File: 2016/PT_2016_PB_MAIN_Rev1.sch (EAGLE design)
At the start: 113 parts, among them Q1 Q_IRFS7437PbF, Q11 Q_IRFS7437PbF, Q12 2N7002, Q14 Q_IRFS7437PbF, Q16 Q_IRFS7437PbF, Q20 Q_IRFS7437PbF, Q6 Q_IRFS7437PbF, Q7 Q_IRFS7437PbF, Q9 Q_IRFS7437PbF

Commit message: Added Murata 5V Converter and TI uC
Rearranged board
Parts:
- removed 12V-CRIT: H_WR-TBL_3210002HORIZ, MRDT-2015-PowerBoard:H_WR-TBL_3210002HORIZ
- removed JP1: (no value), jumper:JP1E
- removed LED13: (no value), SparkFun-LED:LED-FKIT-1206
- removed LED3: (no value), SparkFun-LED:LED1206
- removed R11: 1kΩ, SparkFun-Passives:RESISTOR1206
- removed R2: 10k Ohm, SparkFun-Passives:RESISTOR1206
- added C10: 1uF, resistor:C-USC1206
- added OKI-78SR-5/1.5-W36H: Q_OKI-78SR, MRDT-2015-PowerBoard:Q_OKI-78SR
- added R6: 120 Ohm, SparkFun-Passives:RESISTOR1206
- added U$12: MAX3077, MAX3077:MAX3077
- added U$23, U$5: RJ45-8PTH, SparkFun-Connectors:RJ45-8PTH
- added U$3: MURATA_5V_DC-DC_CONVERTER, Murata_5V_DC-DC_Converter:MURATA_5V_DC-DC_CONVERTER
- added U$4: TIVA-C-CONNECTED, MRDT-2015-General:TIVA-C-CONNECTED
- R1: value 1k Ohm -> 120 Ohm
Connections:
- removed net 12V-CRIT: 12V-CRIT.R, LED3.A
- removed net INFO_LED: R1.1
- removed net JUMPER_SIG_IN: JP1.1, R2.1
- removed net N$11: LED13.A, R1.2
- new net N$18: R6.1, U$12.Z, U$5.2
- new net N$19: R1.2, U$12.B, U$5.6
- new net N$20: R1.1, U$12.A, U$5.3
- new net N$21: U$12.DI
- new net RXD: U$12.R0
- net +5V: now also C10.1, U$12.VCC; no longer R2.2
- net GND: now also C10.2, U$12.GND, U$5.7, U$5.8; no longer 12V-CRIT.L, JP1.2, LED13.C, R11.2
- net N$3: now also R6.2, U$12.Y, U$5.1; no longer LED3.C, R11.1
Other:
- moved on the sheet: 5V-INT, LED5, R1, R13

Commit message: Added final components and started routing.
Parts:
- added 5V-AUX: H_20020618-M02HORIZ, MRDT-2015-PowerBoard:H_20020618-M02HORIZ
- added LED3: (no value), SparkFun-LED:LED1206
- added R2, R7: 120 Ohm, SparkFun-Passives:RESISTOR1206
- added R8: 1kΩ, SparkFun-Passives:RESISTOR1206
- added U$24: MAX3077, MAX3077:MAX3077
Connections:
- new net 5V-AUX: 5V-AUX.R, R8.1
- new net 5V_AUX: U$3.+VOUT
- new net AUX_P2-IMEAS: U$2.VIOUT, U$4.PM6
- new net AUX_P2-SIG: U$1.IN, U$4.PD2
- new net N$100: U$4.RST
- new net N$101: U$4.PB2
- new net N$102: U$4.PB3
- new net N$105: U$4.PD0
- new net N$106: U$4.PD1
- new net N$108: U$4.PD3
- new net N$109: U$4.PD4
- new net N$11: R2.2, U$23.6, U$24.B
- new net N$110: U$4.PD5
- new net N$111: U$4.PD7
- new net N$112: U$4.PE0
- new net N$113: U$4.PE1
- new net N$115: U$4.PE2
- new net N$116: U$4.PE3
- new net N$117: U$4.PE4
- new net N$118: U$4.PE5
- new net N$119: U$4.PG0
- new net N$120: U$4.PG1
- new net N$121: U$4.PL0
- new net N$122: U$4.PL1
- new net N$123: U$4.PL2
- new net N$124: U$4.PL3
- new net N$125: U$4.PL4
- new net N$126: U$4.PL5
- new net N$127: U$4.PN2
- new net N$128: U$4.PN3
- new net N$129: U$4.PN4
- new net N$130: U$4.PN5
- new net N$131: U$4.PQ0
- new net N$133: U$4.PQ2/PA3
- new net N$134: U$4.PQ3/PA2
- new net N$32: R2.1, U$23.3, U$24.A
- new net N$33: U$24.DI
- new net N$34: LED3.A, R8.2
- new net N$35: U$4.PA4
- new net N$36: U$4.PA5
- new net N$37: U$4.PA6
- new net N$43: U$4.PC4
- new net N$48: U$4.PC5
- new net N$5: R7.2, U$23.1, U$24.Y
- new net N$50: U$4.PC6
- new net N$51: U$4.PC7
- new net N$52: U$4.PF1
- new net N$53: U$4.PF2
- new net N$58: U$4.PF3
- new net N$65: U$4.PH2
- new net N$70: U$4.PH3
- new net N$75: U$4.PK4
- new net N$76: U$4.PK5
- new net N$8: R7.1, U$23.2, U$24.Z
- new net N$83: U$4.PM0
- new net N$84: U$4.PM1
- new net N$85: U$4.PM2
- new net N$86: U$4.PM3
- new net N$87: U$4.PM4
- new net N$88: U$4.PM5
- new net N$90: U$4.PM7
- new net N$91: U$4.PP0
- new net N$92: U$4.PP1
- new net N$93: U$4.PP2
- new net N$97: U$4.+5V
- new net N$98: U$4.+3V3
- new net N$99: U$4.GND
- new net RXD1: U$24.R0
- net +5V: now also OKI-78SR-5/1.5-W36H.VO, U$24.VCC
- net AUX_P-IMEAS: now also U$4.PK7; no longer U$2.VIOUT
- net AUX_P-SIG: now also U$4.PB4; no longer U$1.IN
- net GND: now also 5V-AUX.L, LED3.C, OKI-78SR-5/1.5-W36H.GND, U$23.7, U$23.8, U$24.GND, U$3.-VIN, U$3.-VOUT
- net M1-IMEAS: now also U$4.PA7
- net M1-SIG: now also U$4.PP4
- net M2-IMEAS: now also U$4.PH0
- net M2-SIG: now also U$4.PK3
- net M3-IMEAS: now also U$4.PH1
- net M3-SIG: now also U$4.PK2
- net M4-IMEAS: now also U$4.PP3
- net M4-SIG: now also U$4.PK1
- net M5-IMEAS: now also U$4.PK6
- net M5-SIG: now also U$4.PK0
- net M6-IMEAS: now also U$4.PQ1
- net M6-SIG: now also U$4.PB5
- net V_BATT: now also OKI-78SR-5/1.5-W36H.VI, U$3.+VIN
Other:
- moved on the sheet: C10, OKI-78SR-5/1.5-W36H, U$23, U$3

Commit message: Continued routing, rearranged some things
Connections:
- removed net 5V_AUX: U$3.+VOUT
- removed net N$21: U$12.DI
- removed net N$33: U$24.DI
- removed net N$43: U$4.PC4
- removed net N$48: U$4.PC5
- removed net N$65: U$4.PH2
- removed net N$91: U$4.PP0
- removed net N$92: U$4.PP1
- removed net N$93: U$4.PP2
- removed net N$97: U$4.+5V
- removed net N$99: U$4.GND
- removed net RXD: U$12.R0
- removed net RXD1: U$24.R0
- new net RX1: U$12.R0, U$4.PC4
- new net RX2: U$24.R0, U$4.PP0
- new net TX1: U$12.DI, U$4.PC5
- new net TX2: U$24.DI, U$4.PP1
- net +5V: now also U$4.+5V
- net 12V-IMEAS: now also U$4.PH2
- net 5V-AUX: now also U$3.+VOUT
- net GND: now also U$4.GND
- net PRIMARY-VMEAS: now also U$4.PP2
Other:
- moved on the sheet: C10, OKI-78SR-5/1.5-W36H, R1, R2, R6, R7, U$23, U$5

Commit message: Routesss
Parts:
- removed U$22: TEST, MRDT-2015-General:TEST
- renumbered PALPATINE-12V to POE-12V, SIDEOUS-12V to FINN-12V, U$3 to REY-5V
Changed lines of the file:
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@@
 </classes>
 <parts>
-<part name="SIDEOUS-12V" library="MRDT-2015-PowerBoard" deviceset="UQW-12/20-T48NBS" device=""/>
-<part name="PALPATINE-12V" library="MRDT-2015-PowerBoard" deviceset="UQW-12/20-T48NBS" device=""/>
+<part name="FINN-12V" library="MRDT-2015-PowerBoard" deviceset="UQW-12/20-T48NBS" device=""/>
+<part name="POE-12V" library="MRDT-2015-PowerBoard" deviceset="UQW-12/20-T48NBS" device=""/>
 <part name="GND3" library="SparkFun-Aesthetics" deviceset="GND" device=""/>
 <part name="GND4" library="SparkFun-Aesthetics" deviceset="GND" device=""/>
@@
 <part name="P+25" library="supply1" deviceset="+5V" device=""/>
 <part name="GND95" library="SparkFun-Aesthetics" deviceset="GND" device=""/>
-<part name="U$22" library="MRDT-2015-General" deviceset="TEST" device=""/>
 <part name="SUPPLY2" library="SparkFun-Aesthetics" deviceset="V_BATT" device=""/>
 <part name="Q1" library="MRDT-2015-PowerBoard" deviceset="Q_IRF*7437" device="SMD" value="Q_IRFS7437PbF"/>
@@
 <part name="C9" library="resistor" deviceset="C-US" device="C1206" value="1nF"/>
 <part name="GND13" library="SparkFun-Aesthetics" deviceset="GND" device=""/>
-<part name="U$3" library="Murata_5V_DC-DC_Converter" deviceset="MURATA_5V_DC-DC_CONVERTER" device=""/>
+<part name="REY-5V" library="Murata_5V_DC-DC_Converter" deviceset="MURATA_5V_DC-DC_CONVERTER" device=""/>
 <part name="U$4" library="MRDT-2015-General" deviceset="TIVA-C-CONNECTED" device=""/>
 <part name="U$5" library="SparkFun-Connectors" deviceset="RJ45-8" device="PTH"/>
@@
 </plain>
 <instances>
-<instance part="SIDEOUS-12V" gate="G$1" x="63.5" y="73.66"/>
-<instance part="PALPATINE-12V" gate="G$1" x="63.5" y="43.18"/>
+<instance part="FINN-12V" gate="G$1" x="63.5" y="73.66"/>
+<instance part="POE-12V" gate="G$1" x="63.5" y="43.18"/>
 <instance part="GND3" gate="1" x="35.56" y="30.48"/>
 <instance part="GND4" gate="1" x="35.56" y="60.96"/>
@@
 <instance part="P+25" gate="1" x="226.06" y="91.44"/>
 <instance part="GND95" gate="1" x="226.06" y="66.04"/>
-<instance part="U$22" gate="G$1" x="-1163.32" y="-378.46"/>
 <instance part="SUPPLY2" gate="G$1" x="-518.16" y="231.14"/>
 <instance part="Q1" gate="G$1" x="-520.7" y="182.88"/>
@@
 <instance part="C9" gate="G$1" x="-474.98" y="203.2"/>
 <instance part="GND13" gate="1" x="-487.68" y="231.14"/>
-<instance part="U$3" gate="G$1" x="109.22" y="129.54"/>
+<instance part="REY-5V" gate="G$1" x="109.22" y="129.54"/>
 <instance part="U$4" gate="G$1" x="-162.56" y="-147.32"/>
 <instance part="U$5" gate="G$1" x="-462.28" y="-53.34" rot="R180"/>
@@
 <net name="GND" class="0">
 <segment>
-<pinref part="SIDEOUS-12V" gate="G$1" pin="-VIN"/>
+<pinref part="FINN-12V" gate="G$1" pin="-VIN"/>
 <pinref part="GND4" gate="1" pin="GND"/>
 <wire x1="40.64" y1="66.04" x2="35.56" y2="66.04" width="0.1524" layer="91"/>
@@
 </segment>
 <segment>
-<pinref part="PALPATINE-12V" gate="G$1" pin="-VIN"/>
+<pinref part="POE-12V" gate="G$1" pin="-VIN"/>
 <wire x1="40.64" y1="35.56" x2="35.56" y2="35.56" width="0.1524" layer="91"/>
 <wire x1="35.56" y1="35.56" x2="35.56" y2="33.02" width="0.1524" layer="91"/>
@@
 </segment>
 <segment>
-<pinref part="SIDEOUS-12V" gate="G$1" pin="-VOUT"/>
+<pinref part="FINN-12V" gate="G$1" pin="-VOUT"/>
 <pinref part="GND11" gate="1" pin="GND"/>
 </segment>
 <segment>
-<pinref part="PALPATINE-12V" gate="G$1" pin="-VOUT"/>
+<pinref part="POE-12V" gate="G$1" pin="-VOUT"/>
 <pinref part="GND12" gate="1" pin="GND"/>
 </segment>
@@
 </segment>
 <segment>
-<pinref part="U$3" gate="G$1" pin="-VIN"/>
+<pinref part="REY-5V" gate="G$1" pin="-VIN"/>
 <pinref part="GND19" gate="1" pin="GND"/>
 <wire x1="93.98" y1="127" x2="76.2" y2="127" width="0.1524" layer="91"/>
 <wire x1="76.2" y1="127" x2="76.2" y2="124.46" width="0.1524" layer="91"/>
-<pinref part="U$3" gate="G$1" pin="-VOUT"/>
+<pinref part="REY-5V" gate="G$1" pin="-VOUT"/>
 <wire x1="76.2" y1="124.46" x2="76.2" y2="121.92" width="0.1524" layer="91"/>
 <wire x1="93.98" y1="124.46" x2="76.2" y2="124.46" width="0.1524" layer="91"/>
@@
 <pinref part="SUPPLY3" gate="G$1" pin="V_BATT"/>
 <wire x1="35.56" y1="81.28" x2="35.56" y2="83.82" width="0.1524" layer="91"/>
-<pinref part="SIDEOUS-12V" gate="G$1" pin="+VIN"/>
+<pinref part="FINN-12V" gate="G$1" pin="+VIN"/>
 <wire x1="35.56" y1="81.28" x2="40.64" y2="81.28" width="0.1524" layer="91"/>
 </segment>
@@
 <wire x1="33.02" y1="50.8" x2="33.02" y2="53.34" width="0.1524" layer="91"/>
 <junction x="33.02" y="50.8"/>
-<pinref part="PALPATINE-12V" gate="G$1" pin="+VIN"/>
+<pinref part="POE-12V" gate="G$1" pin="+VIN"/>
 <junction x="33.02" y="50.8"/>
 <wire x1="40.64" y1="50.8" x2="33.02" y2="50.8" width="0.1524" layer="91"/>
@@
 </segment>
 <segment>
-<pinref part="U$3" gate="G$1" pin="+VIN"/>
+<pinref part="REY-5V" gate="G$1" pin="+VIN"/>
 <pinref part="SUPPLY5" gate="G$1" pin="V_BATT"/>
 <wire x1="93.98" y1="132.08" x2="76.2" y2="132.08" width="0.1524" layer="91"/>
@@
 <net name="N$4" class="0">
 <segment>
-<pinref part="PALPATINE-12V" gate="G$1" pin="REMOTE"/>
+<pinref part="POE-12V" gate="G$1" pin="REMOTE"/>
 <wire x1="40.64" y1="43.18" x2="15.24" y2="43.18" width="0.1524" layer="91"/>
 <wire x1="15.24" y1="43.18" x2="15.24" y2="58.42" width="0.1524" layer="91"/>
-<pinref part="SIDEOUS-12V" gate="G$1" pin="REMOTE"/>
+<pinref part="FINN-12V" gate="G$1" pin="REMOTE"/>
 <wire x1="15.24" y1="58.42" x2="15.24" y2="73.66" width="0.1524" layer="91"/>
 <wire x1="15.24" y1="73.66" x2="40.64" y2="73.66" width="0.1524" layer="91"/>
@@
 <net name="N$7" class="0">
 <segment>
-<pinref part="PALPATINE-12V" gate="G$1" pin="+VOUT"/>
+<pinref part="POE-12V" gate="G$1" pin="+VOUT"/>
 <wire x1="88.9" y1="50.8" x2="96.52" y2="50.8" width="0.1524" layer="91"/>
 <wire x1="96.52" y1="50.8" x2="96.52" y2="53.34" width="0.1524" layer="91"/>
-<pinref part="SIDEOUS-12V" gate="G$1" pin="+VOUT"/>
+<pinref part="FINN-12V" gate="G$1" pin="+VOUT"/>
 <wire x1="96.52" y1="53.34" x2="96.52" y2="81.28" width="0.1524" layer="91"/>
 <wire x1="96.52" y1="81.28" x2="88.9" y2="81.28" width="0.1524" layer="91"/>
@@
 </segment>
 <segment>
-<pinref part="U$3" gate="G$1" pin="+VOUT"/>
+<pinref part="REY-5V" gate="G$1" pin="+VOUT"/>
 <wire x1="127" y1="132.08" x2="132.08" y2="132.08" width="0.1524" layer="91"/>
 <label x="132.08" y="132.08" size="1.778" layer="95" xref="yes"/>

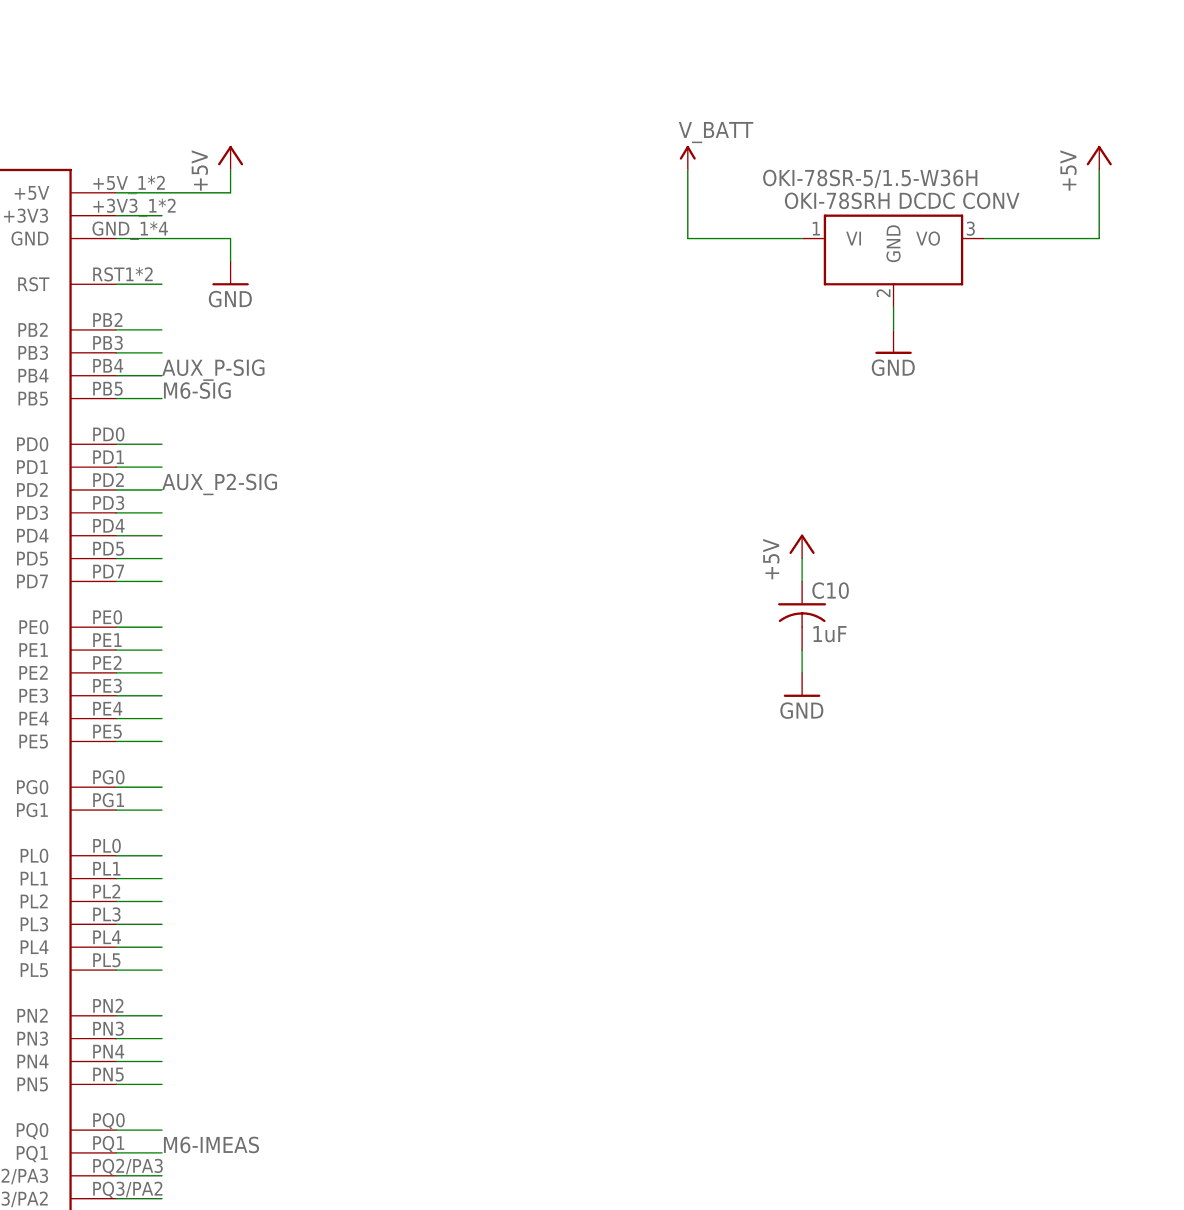
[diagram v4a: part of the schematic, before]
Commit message: Minor routing changes
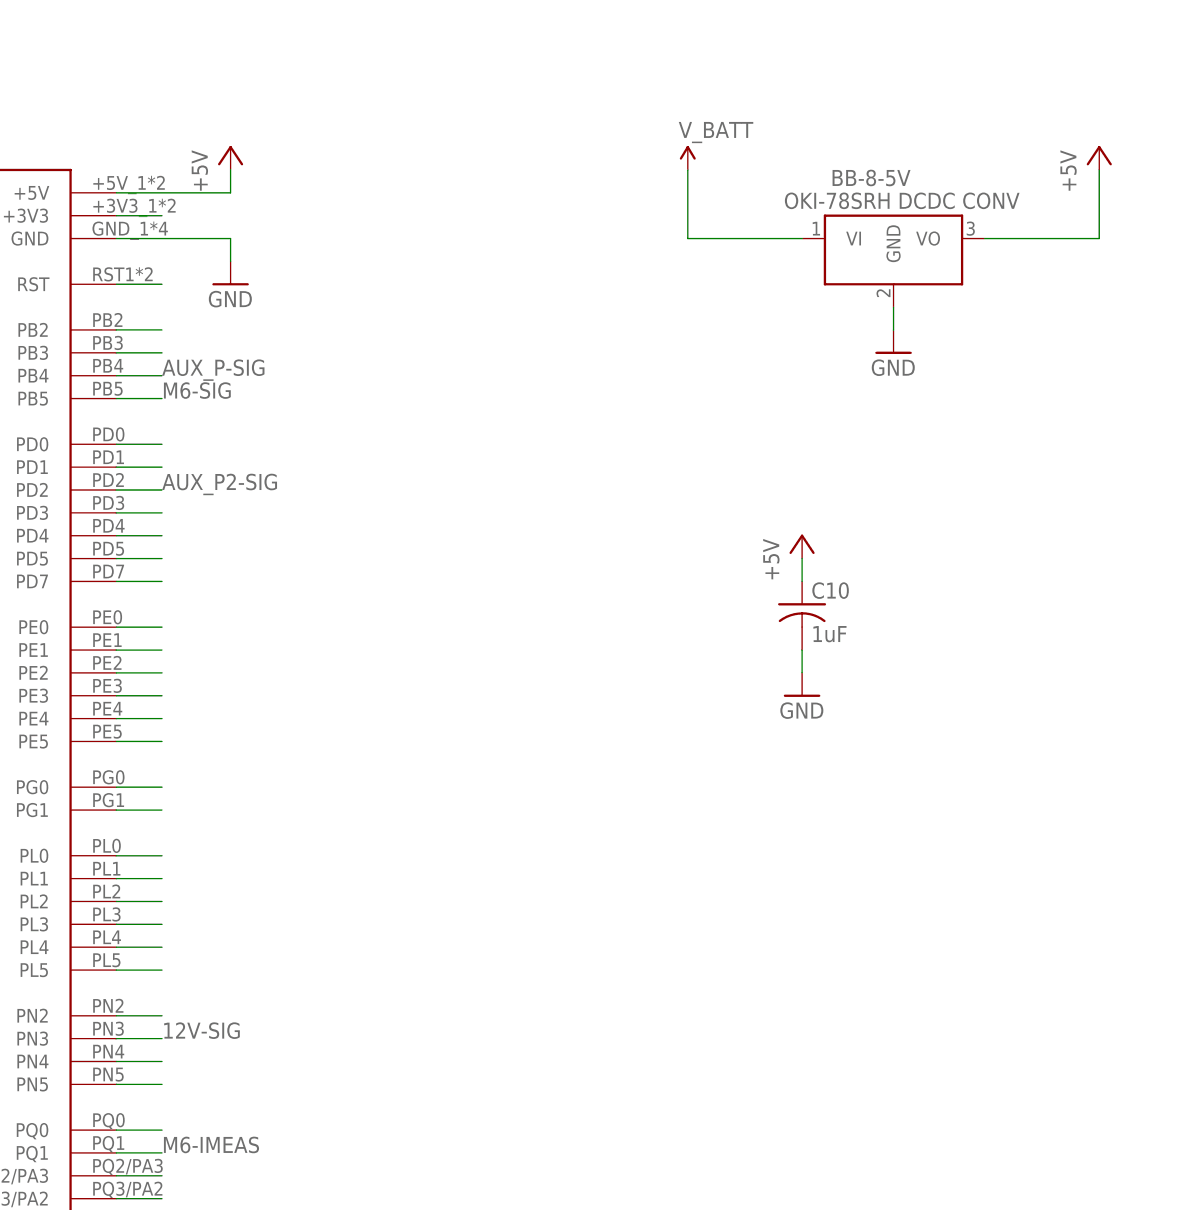
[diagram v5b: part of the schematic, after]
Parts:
- renumbered OKI-78SR-5/1.5-W36H to BB-8-5V
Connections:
- removed net N$128: U$4.PN3
- net 12V-SIG: now also U$4.PN3

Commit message: Rearranged components and routing
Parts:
- added C11: .1µF, resistor:C-USC1206
- added C12: 1nF, resistor:C-USC1206
- added C22: 10µF, resistor:CPOL-USE5-8.5
- added Q2: 2N7002, SparkFun-DiscreteSemi:MOSFET-NCHANNEL2N7002PW
- added R11: 1k, resistor:R-US_R1206
- added U$3: ACS714LLCTR-50A-T, MRDT-2015-PowerBoard:Q_ACS714
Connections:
- removed net N$105: U$4.PD0
- removed net N$106: U$4.PD1
- removed net N$109: U$4.PD4
- removed net N$111: U$4.PD7
- new net 5V-IMEAS: U$3.VIOUT, U$4.PD0
- new net 5V-SIG: R11.2, U$4.PN3
- new net N$38: C12.1, U$3.FILTER
- new net N$43: Q2.D, REY-5V.ON/OFF
- new net N$48: Q2.G, R11.1
- new net N$7: C22.+, REY-5V.+SENSE, REY-5V.+VOUT, U$3.IP+
- new net N$70: U$4.PH2
- new net N$89: U$4.PM6
- new net N$93: U$4.PP4
- net +5V: now also C11.2, U$3.VCC
- net 12V-IMEAS: now also U$4.PD1; no longer U$4.PH2
- net 12V-SIG: now also U$4.PP2; no longer U$4.PN3
- net 5V-AUX: now also U$3.IP-; no longer REY-5V.+VOUT
- net AUX_P-IMEAS: now also U$4.PB4; no longer U$4.PK7
- net AUX_P-SIG: now also U$4.PQ1; no longer U$4.PB4
- net AUX_P2-IMEAS: now also U$4.PD2; no longer U$4.PM6
- net AUX_P2-SIG: now also U$4.PK7; no longer U$4.PD2
- net GND: now also C11.1, C12.2, C22.-, Q2.S, REY-5V.-SENSE, U$3.GND
- net M1-IMEAS: now also U$4.PK3; no longer U$4.PA7
- net M1-SIG: now also U$4.PP5; no longer U$4.PP4
- net M2-IMEAS: now also U$4.PK2; no longer U$4.PH0
- net M2-SIG: now also U$4.PA7; no longer U$4.PK3
- net M3-IMEAS: now also U$4.PK1; no longer U$4.PH1
- net M3-SIG: now also U$4.PH0; no longer U$4.PK2
- net M4-IMEAS: now also U$4.PD4; no longer U$4.PP3
- net M4-SIG: now also U$4.PH1; no longer U$4.PK1
- net M5-IMEAS: now also U$4.PK0; no longer U$4.PK6
- net M5-SIG: now also U$4.PP3; no longer U$4.PK0
- net M6-IMEAS: now also U$4.PB5; no longer U$4.PQ1
- net M6-SIG: now also U$4.PK6; no longer U$4.PB5
- net PRIMARY-VMEAS: now also U$4.PD7; no longer U$4.PP2
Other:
- moved on the sheet: C47, C48, C49, C50, C51, C52, REY-5V
